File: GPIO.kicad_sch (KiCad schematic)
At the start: 10 parts, among them J9 uPD446, K11 74LS273

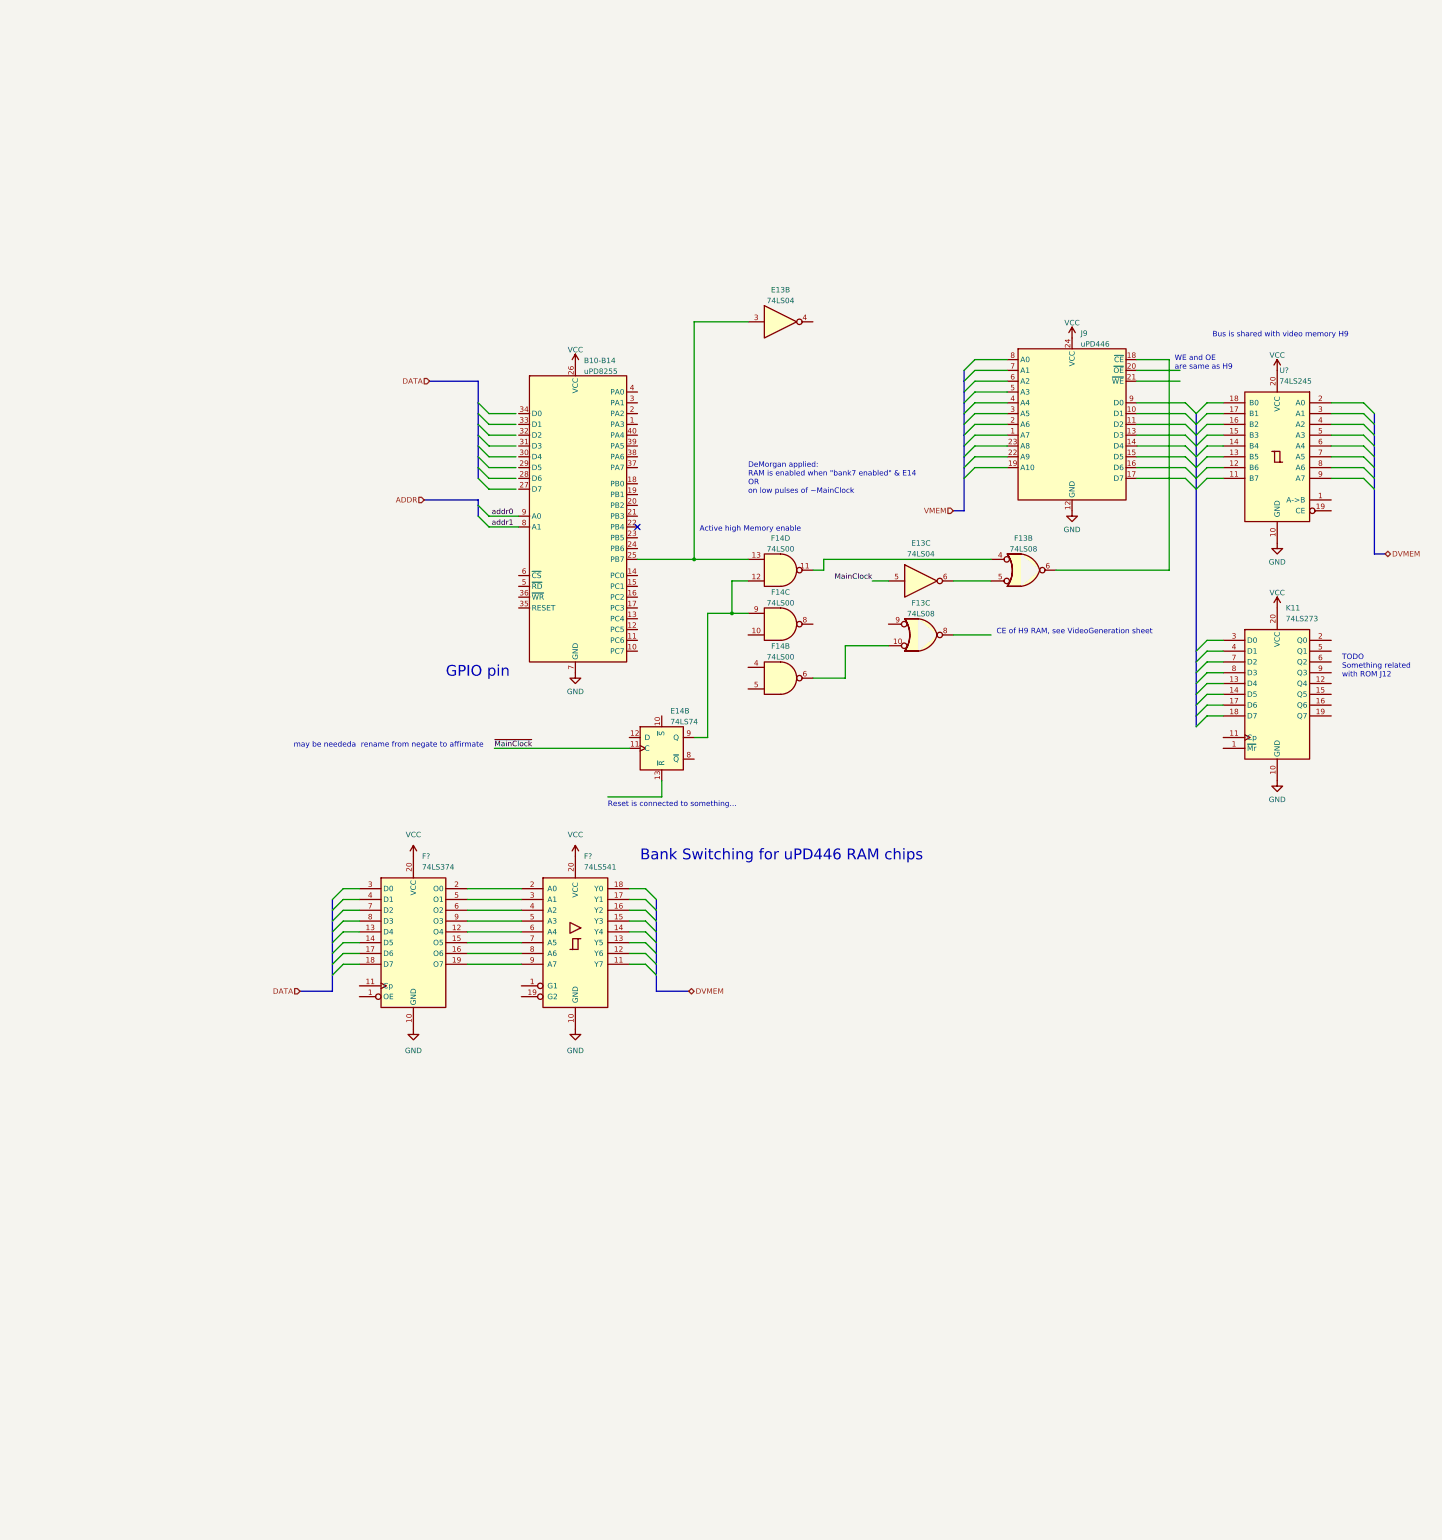
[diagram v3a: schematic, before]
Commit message: Video memory concurrency
- bank7 selector to address video or attribute RAM
- found read and write data paths leading to video RAMs (F11, F12).
- video RAMs CS generation.
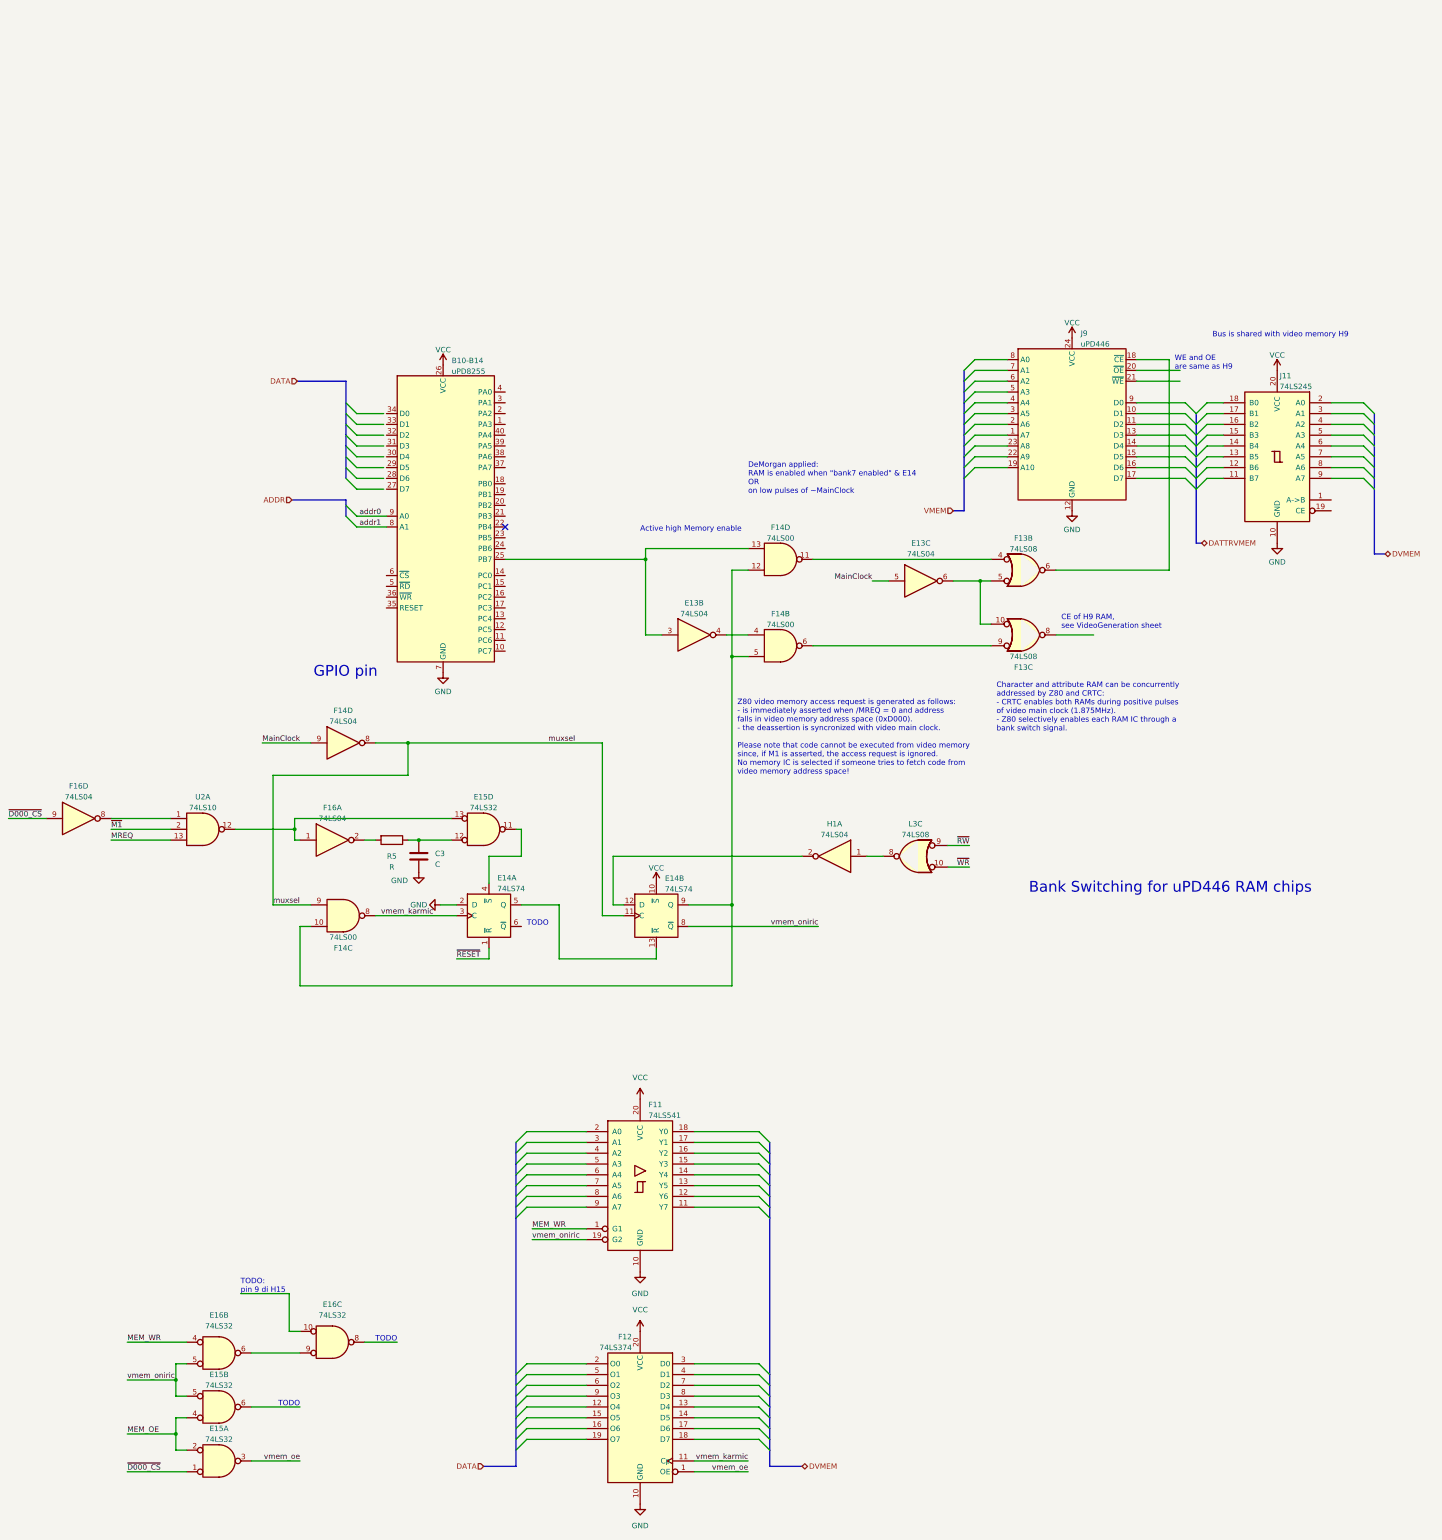
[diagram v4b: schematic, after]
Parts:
- removed K11: 74LS273, symbol 74xx:74LS273
- added C3: C, symbol Device:C
- added unit 1 of E14
- added E15, E16: 74LS32, symbol 74xx:74LS32
- added F14, F16, H1: 74LS04, symbol 74xx:74LS04
- added L3: 74LS08, symbol 74xx:74LS08
- added R5: R, symbol Device:R
- added U2: 74LS10, symbol 74xx:74LS10
- gave numbers to parts that had none: 3
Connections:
- net GND: now also C3.2, E14.2 (D)
- net MainClock: now also F14.9
- net VCC: now also E14.10 (~{S})
- net at F14.4: now also E13.4
- net at F14.5: now also E14.9 (Q), F14.10, F14.12
- net at F14.6: now also F13.9; no longer F13.10
- net at E14.12 (D): now also H1.2
- net at E14.13 (~{R}): now also E14.5 (Q)
- net vmem_oniric: now reaches E14.8 (~{Q})
- net vmem_oniric: now also F11.19 (G2), E15.5, E16.5
- net vmem_karmic: now reaches F14.8
- net vmem_karmic: now also F12.11 (Cp), E14.3 (C)
- net MEM_WR: now reaches F11.1 (G1)
- net MEM_WR: now also E16.4
- net at F11.2 (A0): no longer F12.2 (O0)
- net at F11.3 (A1): no longer F12.5 (O1)
- net at F11.4 (A2): no longer F12.6 (O2)
- net at F11.5 (A3): no longer F12.9 (O3)
- net at F11.6 (A4): no longer F12.12 (O4)
- net at F11.7 (A5): no longer F12.15 (O5)
- net at F11.8 (A6): no longer F12.16 (O6)
- net at F11.9 (A7): no longer F12.19 (O7)
- net vmem_oe: now reaches F12.1 (OE)
- net vmem_oe: now also E15.3
- net at E13.6, F13.5: now also F13.10
- net ~{MainClock} renamed muxsel
- net muxsel: now also F14.9, F14.8
- new net: H1.1, L3.8
- new net: F16.8, U2.1
- new net: E15.13, F16.1, U2.12
- new net: E16.6, E16.9
- new net: C3.1, E15.12, R5.1
- new net: E14.4 (~{S}), E15.11
- new net: F16.2, R5.2
- new net MEM_OE: E15.2, E15.4
- new net MREQ: U2.13
- new net ~{D000_CS}: E15.1, F16.9
- new net ~{M1}: U2.2
- new net ~{RESET}: E14.1 (~{R})
- new net ~{RW}: L3.9
- new net ~{WR}: L3.10
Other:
- note added: "Character and attribute RAM can be concurrently addressed by Z80 and CRTC: - CRTC enables both RAMs during positive pulses of video main clock (1.875MHz). - Z80 selectively enables each RAM IC through a bank switch signal."
- note added: "TODO"
- note added: "TODO: pin 9 di H15"
- note added: "Z80 video memory access request is generated as follows: - is immediately asserted when /MREQ = 0 and address falls in video memory address space (0xD000). - the deassertion is syncronized with video main clock. Please note that code cannot be executed from video memory since, if M1 is asserted, the access request is ignored. No memory IC is selected if someone tries to fetch code from video memo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"
- note removed: "Reset is connected to something..."
- note removed: "TODO Something related with ROM J12"
- note removed: "may be neededa rename from negate to affirmate"
- moved on the sheet: B10-B14, E13B, E14B, F11, F12, F13C, F14B, F14D

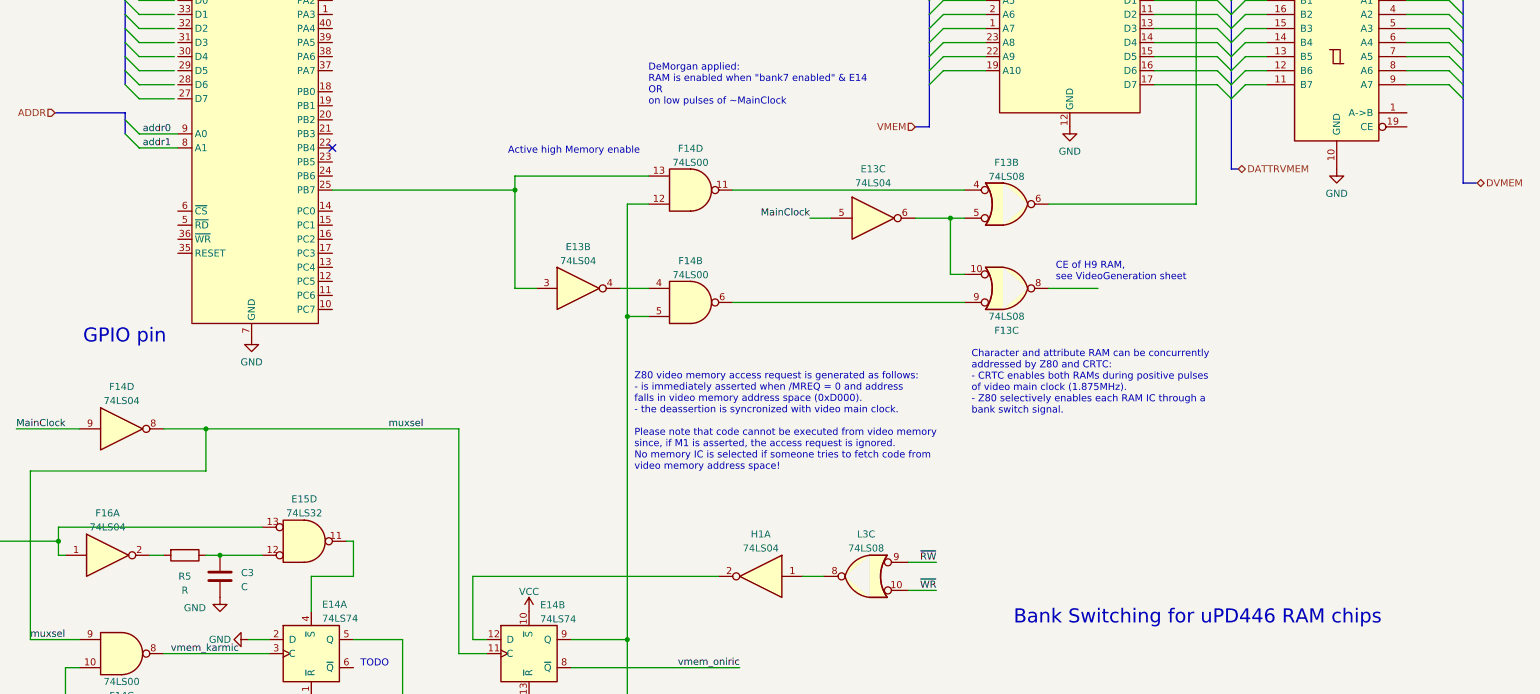
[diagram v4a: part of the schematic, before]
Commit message: Added some missing labels and references
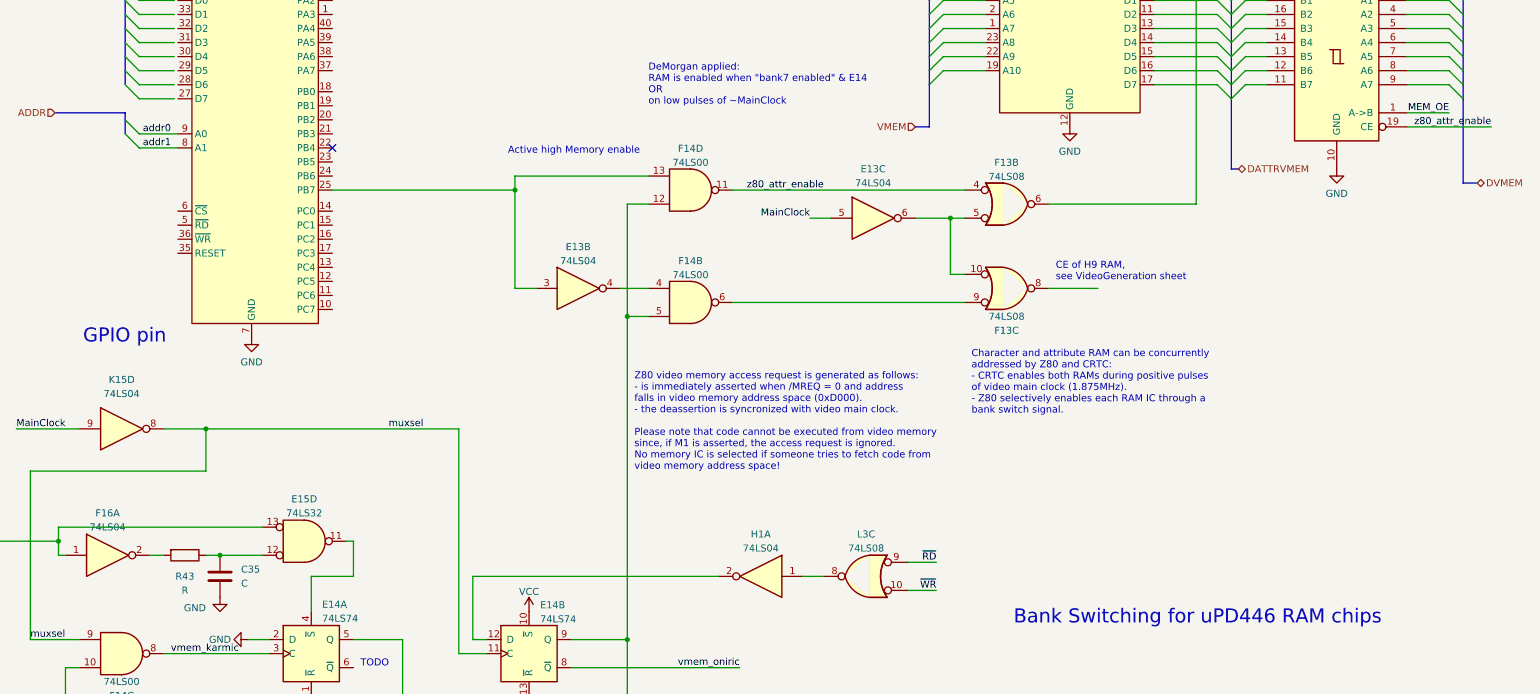
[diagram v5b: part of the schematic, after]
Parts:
- renumbered C3 to C35, F14 to K15, R5 to R43
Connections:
- net MEM_OE: now also J11.1 (A->B)
- net z80_attr_enable: now reaches J11.19 (CE)
- net z80_attr_enable: now also F13.4, F14.11
- net ~{RW} renamed ~{RD}
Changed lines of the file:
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@@
+    (stroke (width 0) (type default))
+  )
+  (wire (pts (xy 279.4 69.85) (xy 264.16 69.85))
     (stroke (width 0) (type default))
   )
@@
   )
   (wire (pts (xy 74.93 280.67) (xy 88.9 280.67))
+    (stroke (width 0) (type default))
+  )
+  (wire (pts (xy 271.78 67.31) (xy 264.16 67.31))
     (stroke (width 0) (type default))
   )
@@
     (effects (font (size 1.27 1.27)) (justify left bottom))
   )
+  (label "z80_attr_enable" (at 279.4 69.85 180) (fields_autoplaced)
+    (effects (font (size 1.27 1.27)) (justify right bottom))
+  )
   (label "~{WR}" (at 179.07 153.67 180) (fields_autoplaced)
     (effects (font (size 1.27 1.27)) (justify right bottom))
@@
     (effects (font (size 1.27 1.27)) (justify left bottom))
   )
+  (label "z80_attr_enable" (at 144.78 81.28 0) (fields_autoplaced)
+    (effects (font (size 1.27 1.27)) (justify left bottom))
+  )
   (label "~{RESET}" (at 58.42 175.26 0) (fields_autoplaced)
     (effects (font (size 1.27 1.27)) (justify left bottom))
@@
     (effects (font (size 1.27 1.27)) (justify left bottom))
   )
-  (label "~{RW}" (at 179.07 148.59 180) (fields_autoplaced)
+  (label "~{RD}" (at 179.07 148.59 180) (fields_autoplaced)
+    (effects (font (size 1.27 1.27)) (justify right bottom))
+  )
+  (label "MEM_OE" (at 271.78 67.31 180) (fields_autoplaced)
     (effects (font (size 1.27 1.27)) (justify right bottom))
   )
@@
   (symbol (lib_id "Device:C") (at 49.53 151.13 0) (unit 1)
     (in_bom yes) (on_board yes) (dnp no) (fields_autoplaced)
-    (property "Reference" "C3" (at 53.34 150.495 0)
+    (property "Reference" "C35" (at 53.34 149.86 0)
       (effects (font (size 1.27 1.27)) (justify left))
     )
-    (property "Value" "C" (at 53.34 153.035 0)
+    (property "Value" "C" (at 53.34 152.4 0)
       (effects (font (size 1.27 1.27)) (justify left))
     )
@@
       (project "ceda"
         (path "/12a6dbe3-008d-4c5b-88f6-9f1c816060be/23c42ab9-740a-4e84-88f1-9f74965e7273"
-          (reference "C3") (unit 1)
+          (reference "C35") (unit 1)
         )
       )
@@
   (symbol (lib_id "Device:R") (at 43.18 147.32 270) (unit 1)
     (in_bom yes) (on_board yes) (dnp no) (fields_autoplaced)
-    (property "Reference" "R5" (at 43.18 151.13 90)
+    (property "Reference" "R43" (at 43.18 151.13 90)
       (effects (font (size 1.27 1.27)))
     )
@@
       (project "ceda"
         (path "/12a6dbe3-008d-4c5b-88f6-9f1c816060be/23c42ab9-740a-4e84-88f1-9f74965e7273"
-          (reference "R5") (unit 1)
+          (reference "R43") (unit 1)
         )
       )
@@
   (symbol (lib_id "74xx:74LS04") (at 31.75 124.46 0) (unit 4)
     (in_bom yes) (on_board yes) (dnp no) (fields_autoplaced)
-    (property "Reference" "F14" (at 31.75 116.84 0)
-      (effects (font (size 1.27 1.27)))
-    )
-    (property "Value" "74LS04" (at 31.75 119.38 0)
+    (property "Reference" "K15" (at 31.75 115.57 0)
+      (effects (font (size 1.27 1.27)))
+    )
+    (property "Value" "74LS04" (at 31.75 118.11 0)
       (effects (font (size 1.27 1.27)))
     )
@@
       (project "ceda"
         (path "/12a6dbe3-008d-4c5b-88f6-9f1c816060be/23c42ab9-740a-4e84-88f1-9f74965e7273"
-          (reference "F14") (unit 4)
-        )
-      )
+          (reference "K15") (unit 4)
+        )
+      )

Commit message: Reset circuit
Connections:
- net RESET: now reaches B10-B14.35 (RESET)
- net ~{CS_IO_GPIO}: now reaches B10-B14.6 (~{CS})
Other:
- note added: "TODO: pin 9 (Q) di H15 (7474)"
- note removed: "TODO: pin 9 di H15"
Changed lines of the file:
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@@
+    (stroke (width 0) (type default))
+  )
+  (wire (pts (xy 30.48 87.63) (xy 41.91 87.63))
     (stroke (width 0) (type default))
   )
@@
     (stroke (width 0) (type default))
   )
+  (wire (pts (xy 30.48 85.09) (xy 41.91 85.09))
+    (stroke (width 0) (type default))
+  )
   (bus (pts (xy 72.39 285.75) (xy 72.39 288.29))
     (stroke (width 0) (type default))
@@
     (stroke (width 0) (type default))
   )
+  (wire (pts (xy 30.48 92.71) (xy 41.91 92.71))
+    (stroke (width 0) (type default))
+  )
   (bus (pts (xy 72.39 273.05) (xy 72.39 275.59))
     (stroke (width 0) (type default))
   )
   (bus (pts (xy 232.41 77.47) (xy 233.68 77.47))
+    (stroke (width 0) (type default))
+  )
+  (wire (pts (xy 30.48 90.17) (xy 41.91 90.17))
     (stroke (width 0) (type default))
   )
@@
     (effects (font (size 1.27 1.27)) (justify left bottom))
   )
-  (text "TODO:\npin 9 di H15" (at 7.62 254 0)
+  (text "TODO:\npin 9 (Q) di H15 (7474)" (at 7.62 254 0)
     (effects (font (size 1.27 1.27)) (justify left bottom))
   )
@@
     (effects (font (size 1.27 1.27)) (justify right bottom))
   )
+  (label "RESET" (at 30.48 92.71 0) (fields_autoplaced)
+    (effects (font (size 1.27 1.27)) (justify left bottom))
+  )
   (label "muxsel" (at 80.01 124.46 0) (fields_autoplaced)
     (effects (font (size 1.27 1.27)) (justify left bottom))
@@
     (effects (font (size 1.27 1.27)) (justify right bottom))
   )
+  (label "~{CS_IO_GPIO}" (at 30.48 85.09 0) (fields_autoplaced)
+    (effects (font (size 1.27 1.27)) (justify left bottom))
+  )
   (label "vmem_oe" (at 127 295.91 180) (fields_autoplaced)
